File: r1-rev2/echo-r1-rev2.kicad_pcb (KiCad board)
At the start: 6 copper layers, 140 x 120.6 mm, 153 parts, among them J1 TYPE-C-31-M-12, J2 TF-115, J3 HP_3.5mm, J4 LO_3.5mm, J5 GT-BTP30003-xxxA-16A, J6 AFC07-S30ECA-00, J7 Conn_SWDUART, J8 BATT, J9 Micro_SD_Card, Q1 AO3401A, Q2 AO3401A, Q3 AO3401A, Q4 AO3401A, Q5 AO3401A, SW1 A, SW10 SELECT, SW11 VOL+, SW12 VOL-, SW13 POWER, SW14 HOLD, SW2 B, SW3 X, SW4 Y, SW5 DPAD↑, SW6 DPAD↓, SW7 DPAD←, SW8 DPAD→, SW9 START, U1 STM32H7R3Z8Jx, U10 USBLC6-2SC6, U11 TPAZ1143-04F, U12 TPAZ1143-04F, U13 TPAZ1143-04F, U14 TPAZ1143-04F, U15 TPAZ1143-04F, U16 TPAZ1143-04F, U2 W958D8NBYA5I, U3 TLV320AIC3104, U4 LM66100DCK, U5 TPS62A01DRLR, U6 TPS62A01DRLR, U7 AP2125K-3.0, U8 AP2125K-3.0, U9 TP4057, Y1 SC-32S32.768kHz20PPM12.5pF, Y2 XTM32024000JT00351001

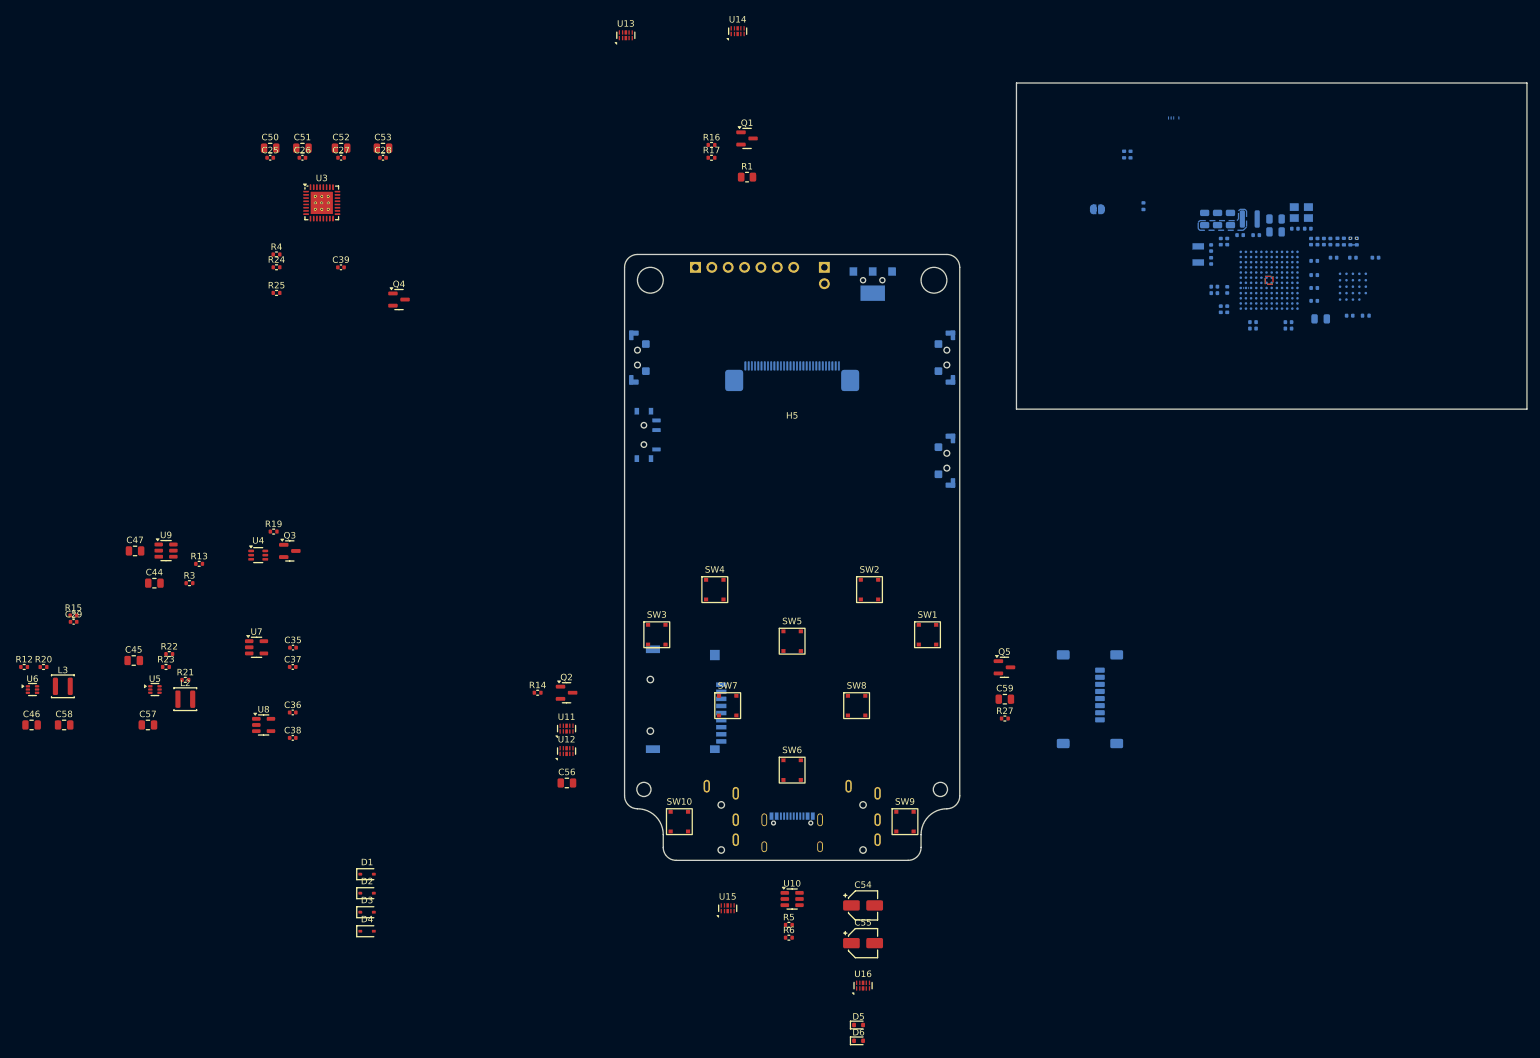
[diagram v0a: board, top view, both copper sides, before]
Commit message: Fix symbol library links & resync footprints from KiCAD libraries
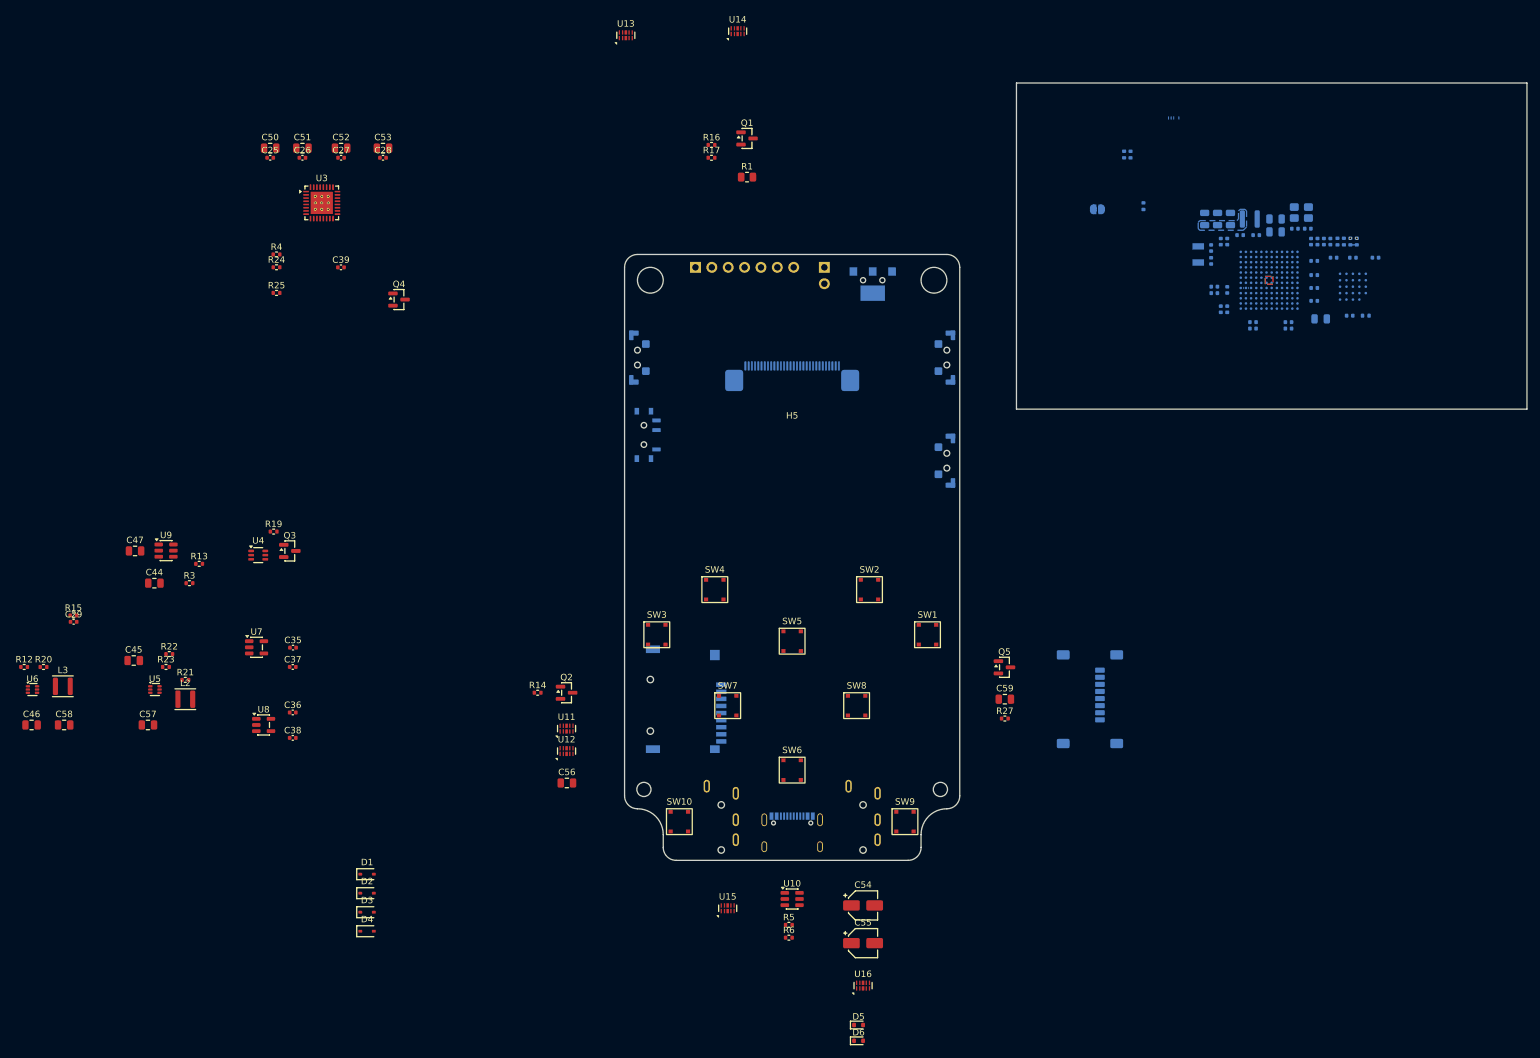
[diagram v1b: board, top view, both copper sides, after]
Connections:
- U1 pad G5: /lcd.dcx -> unconnected-(U1-PC1-PadG5)
- U1 pad L3: unconnected-(U1-PC4-PadL3) -> /lcd.dcx
